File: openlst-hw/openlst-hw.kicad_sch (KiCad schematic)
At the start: 4 parts

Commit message: propate the changes to RF
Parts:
- H1, H2, H3, H4: now not fitted
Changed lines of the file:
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@@
 		(in_bom yes)
 		(on_board yes)
-		(dnp no)
+		(dnp yes)
 		(property "Reference" "H1"
 			(at 154.94 170.2816 90)
@@
 		(in_bom yes)
 		(on_board yes)
-		(dnp no)
+		(dnp yes)
 		(property "Reference" "H2"
 			(at 154.94 175.3616 90)
@@
 		(in_bom yes)
 		(on_board yes)
-		(dnp no)
+		(dnp yes)
 		(property "Reference" "H3"
 			(at 154.94 180.4416 90)
@@
 		(in_bom yes)
 		(on_board yes)
-		(dnp no)
+		(dnp yes)
 		(property "Reference" "H4"
 			(at 154.94 185.5216 90)

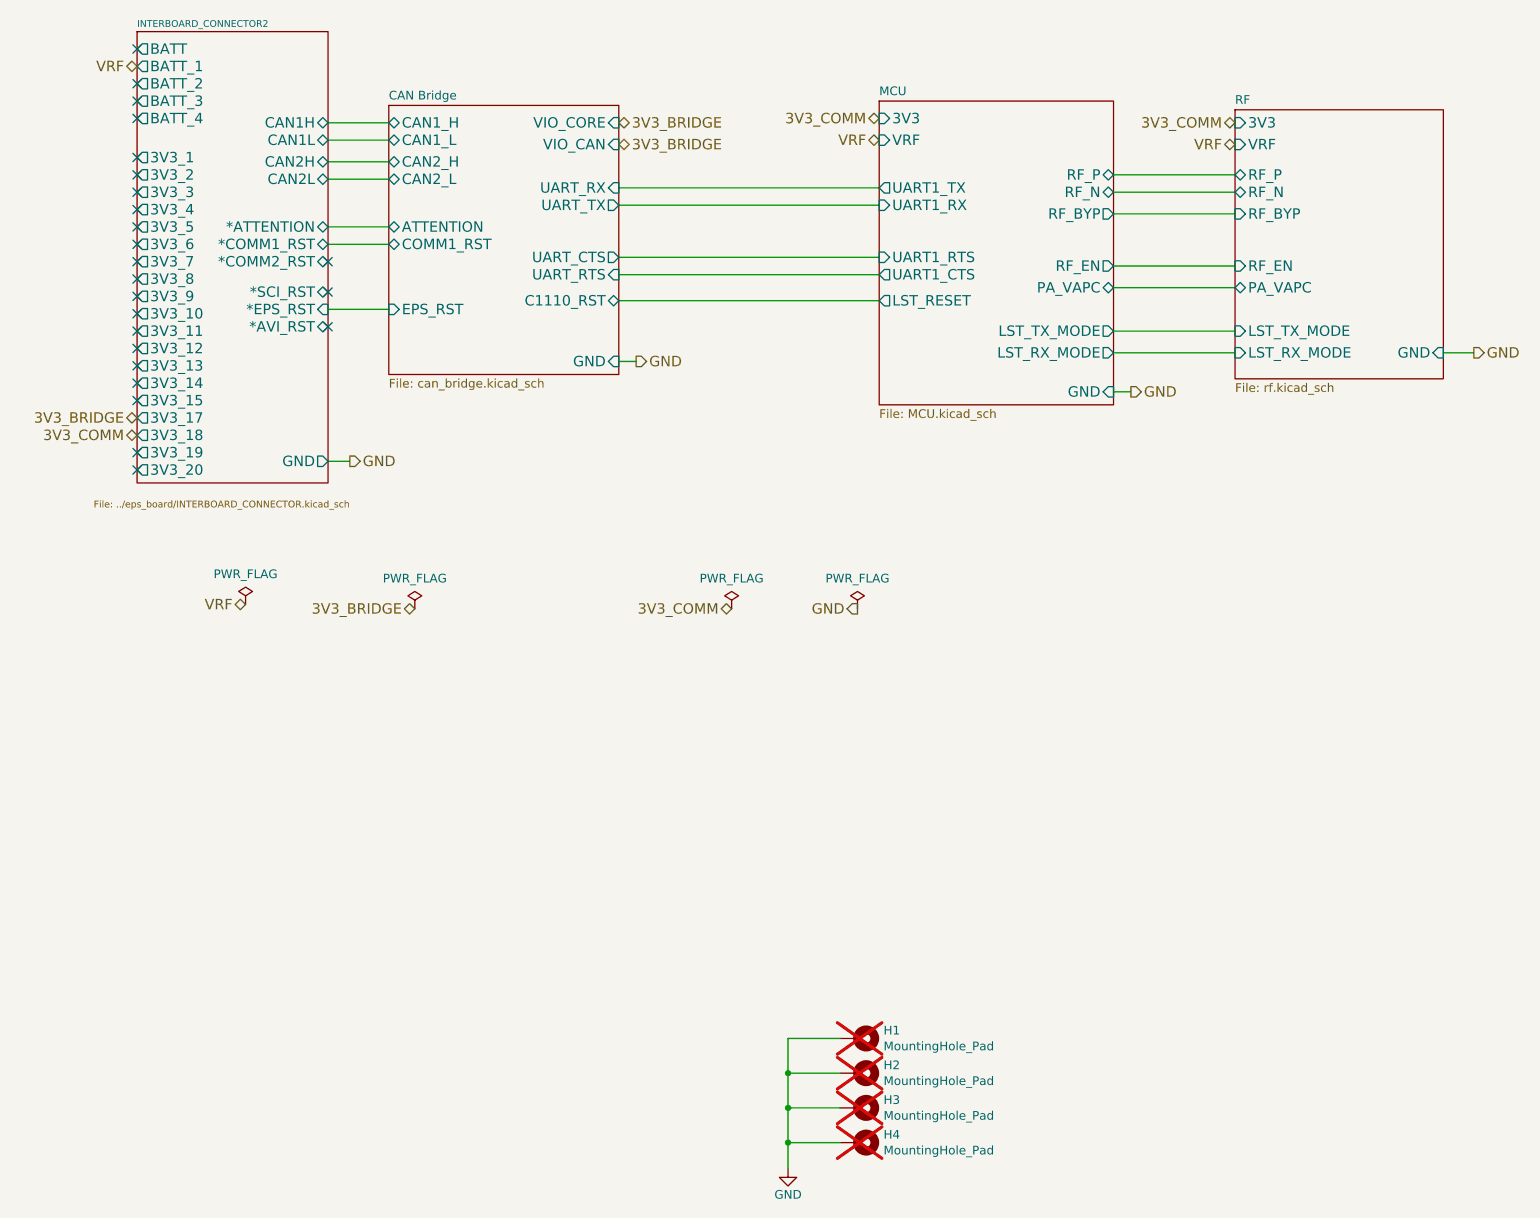
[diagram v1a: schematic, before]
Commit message: local switches and monitors for SCI and RF
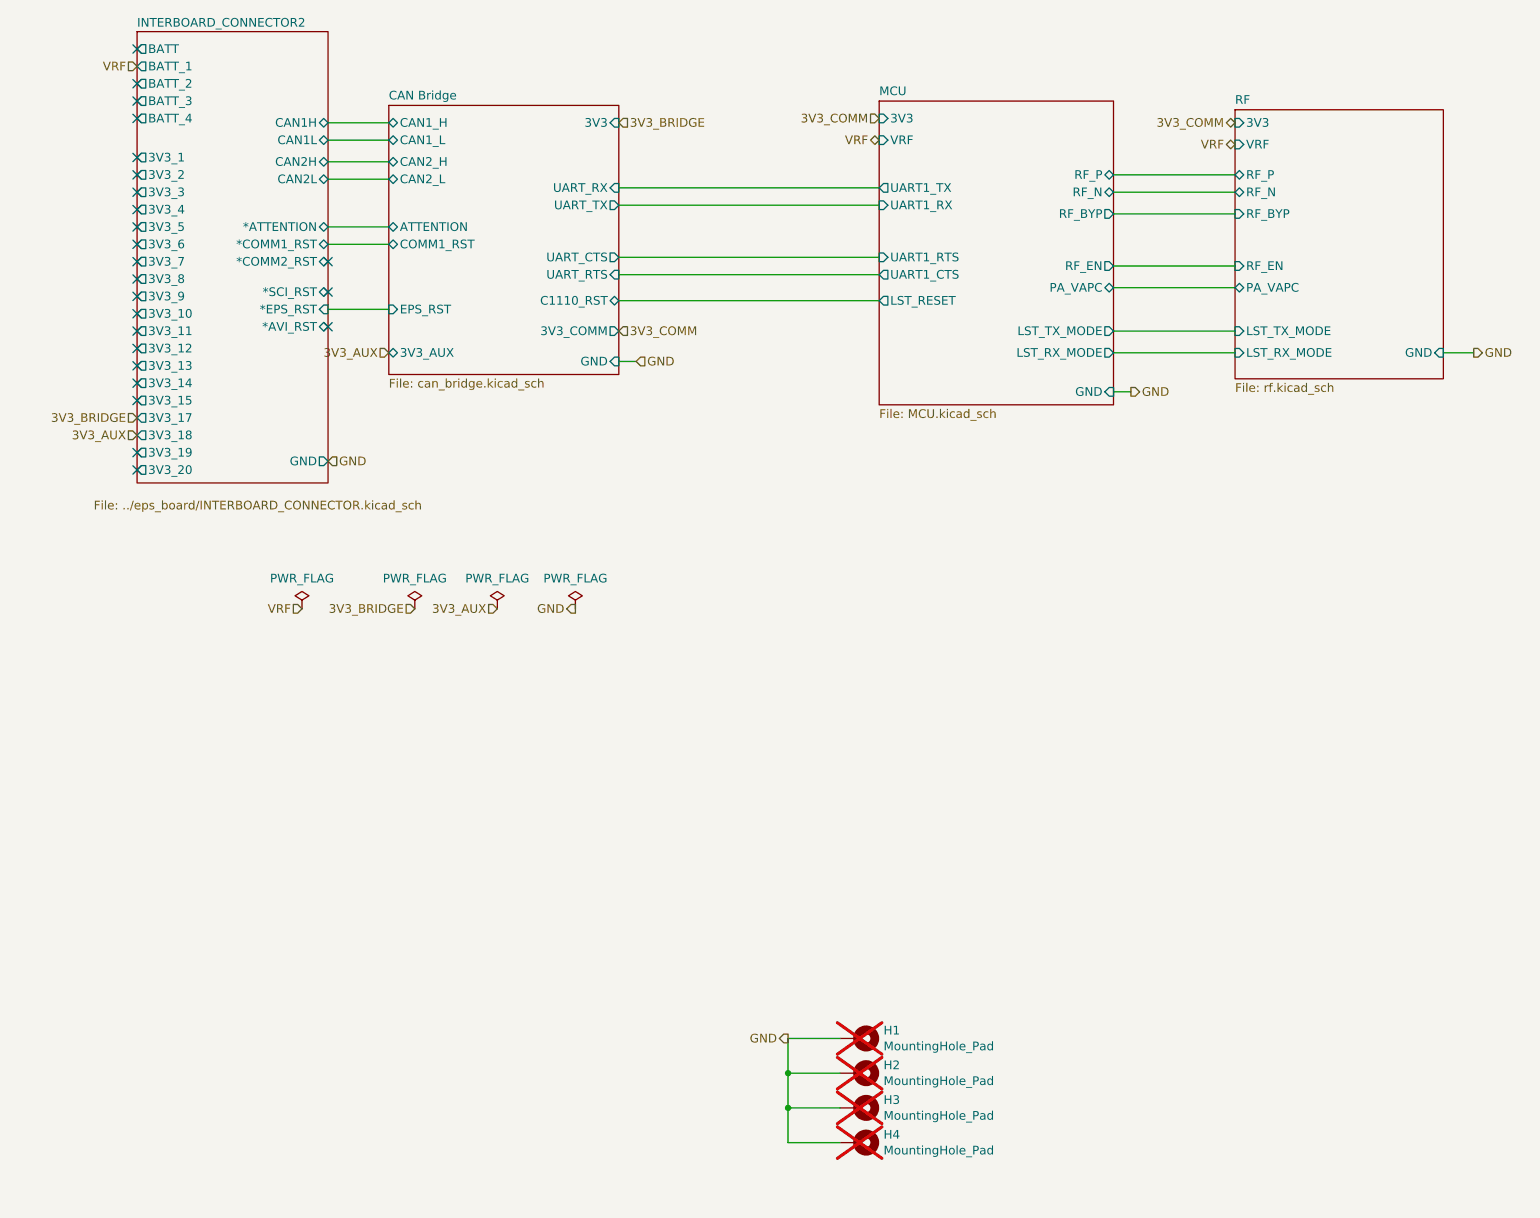
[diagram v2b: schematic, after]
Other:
- sheet CAN Bridge ports: added 3V3, 3V3_AUX, 3V3_COMM; removed VIO_CAN, VIO_CORE
